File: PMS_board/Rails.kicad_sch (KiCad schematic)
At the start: 33 parts, among them J1 D1, J10 CORE, J11 DRIVE, J12 JET1, J13 AUX1, J14 AUX2, J15 JET2, J2 D2, J3 D3, J4 D4, J5 T1, J6 T2, J7 T3, J8 T4, J9 NET

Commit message: Add Footprints & such
whoops forgot to push yesterday teehee
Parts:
- added TP2: TestPoint, Relay_THT:Relay_DPDT_Schrack-RT2-FormC_RM5mm, symbol Connector:TestPoint
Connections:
- net AUX+: now also TP2.1
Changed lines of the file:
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@@
+	)
+	(junction
+		(at 137.16 120.65)
+		(diameter 0)
+		(color 0 0 0 0)
 	)
 	(junction
@@
 					(unit 1)
 				)
+			)
+		)
+	)
+	(symbol
+		(lib_id "Connector:TestPoint")
+		(at 137.16 120.65 0)
+		(unit 1)
+		(body_style 1)
+		(exclude_from_sim no)
+		(in_bom yes)
+		(on_board yes)
+		(in_pos_files yes)
+		(dnp no)
+		(fields_autoplaced yes)
+		(property "Reference" "TP2"
+			(at 139.7 116.0779 0)
+			(show_name no)
+			(do_not_autoplace no)
+			(effects
+				(font
+					(size 1.27 1.27)
+				)
+				(justify left)
+			)
+		)
+		(property "Value" "TestPoint"
+			(at 139.7 118.6179 0)
+			(show_name no)
+			(do_not_autoplace no)
+			(effects
+				(font
+					(size 1.27 1.27)
+				)
+				(justify left)
+			)
+		)
+		(property "Footprint" "Relay_THT:Relay_DPDT_Schrack-RT2-FormC_RM5mm"
+			(at 142.24 120.65 0)
+			(hide yes)
+			(show_name no)
+			(do_not_autoplace no)
+			(effects
+				(font
+					(size 1.27 1.27)
+				)
+			)
+		)
+		(property "Datasheet" ""
+			(at 142.24 120.65 0)
+			(hide yes)
+			(show_name no)
+			(do_not_autoplace no)
+			(effects
+				(font
+					(size 1.27 1.27)
+				)
+			)
+		)
+		(property "Description" "test point"
+			(at 137.16 120.65 0)
+			(hide yes)
+			(show_name no)
+			(do_not_autoplace no)
+			(effects
+				(font
+					(size 1.27 1.27)
+				)
+			)
+		)
+		(pin "1"
+		)
+		(instances
+			(project "PMS_board"
+				(path "/282246b0-e0d8-4997-b3ee-58bf10355d52/266cb597-81f7-4ea7-87c1-e1b826fc674e/1ce466be-8c1f-42c9-b575-af9917f46ea9"
+					(reference "TP2")
+					(unit 1)
+				)

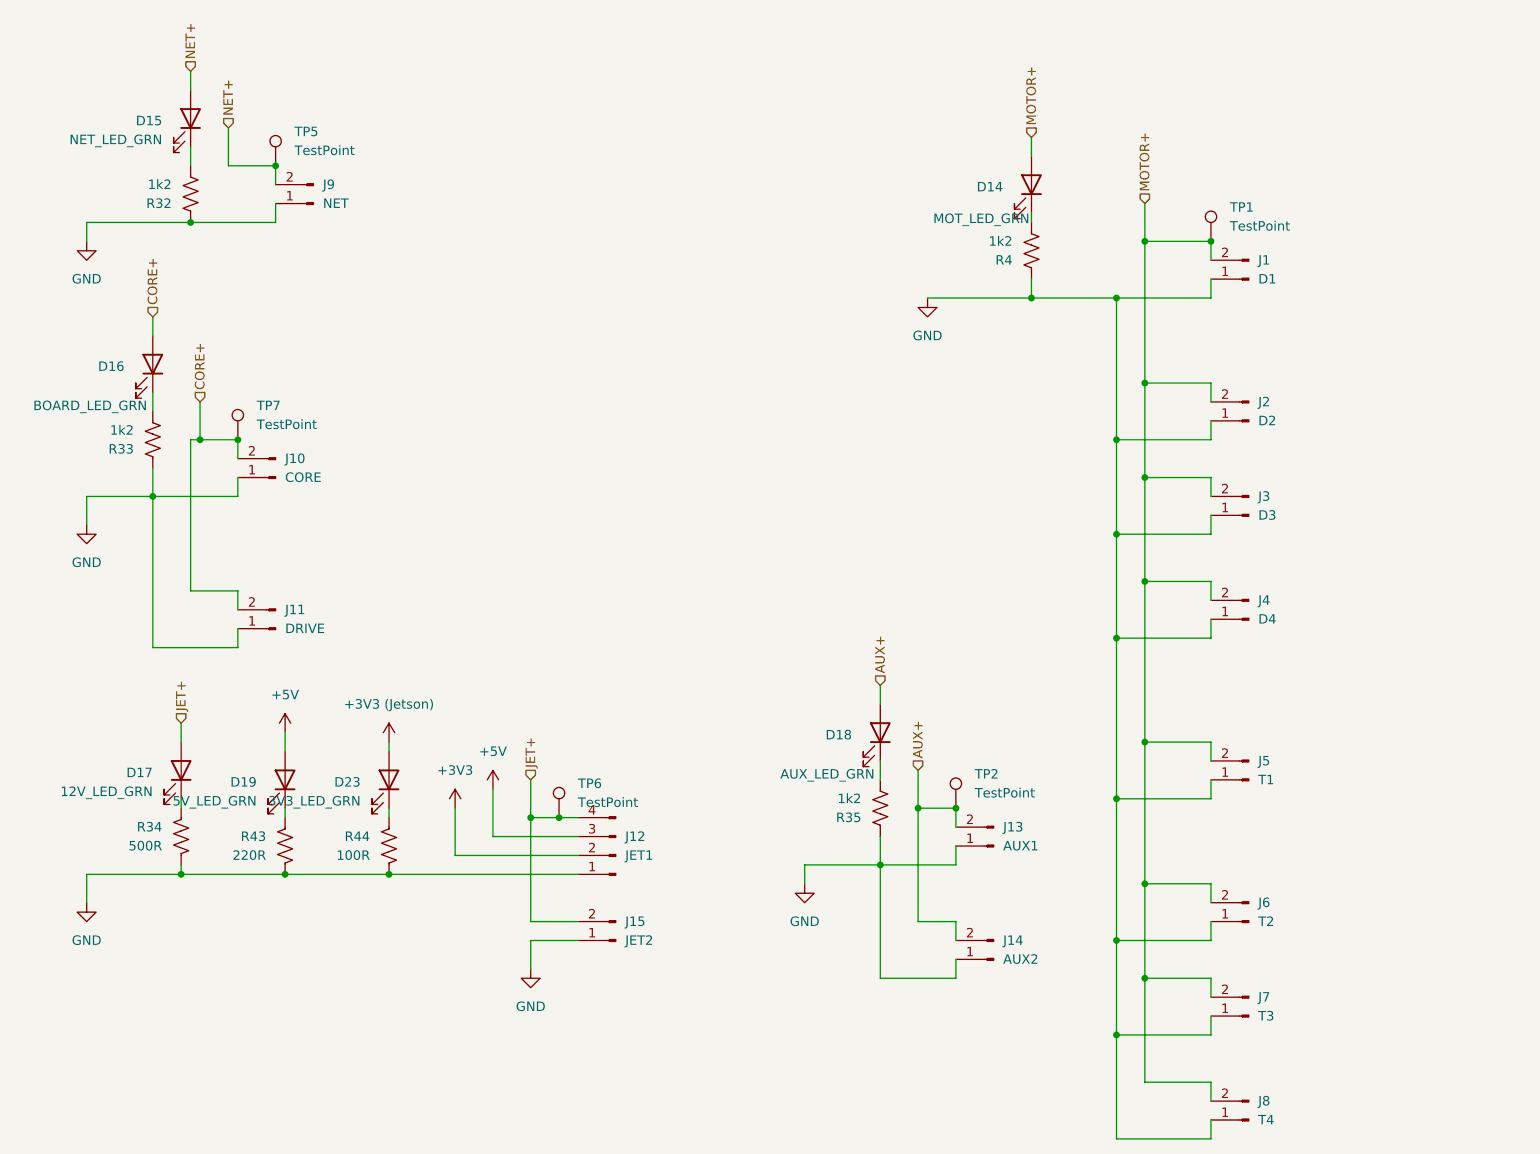
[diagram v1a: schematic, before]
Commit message: Minor component tweaks and added a seperate LED sheet
Changed component values
Added labels
Moved LEDs to it's own sheet
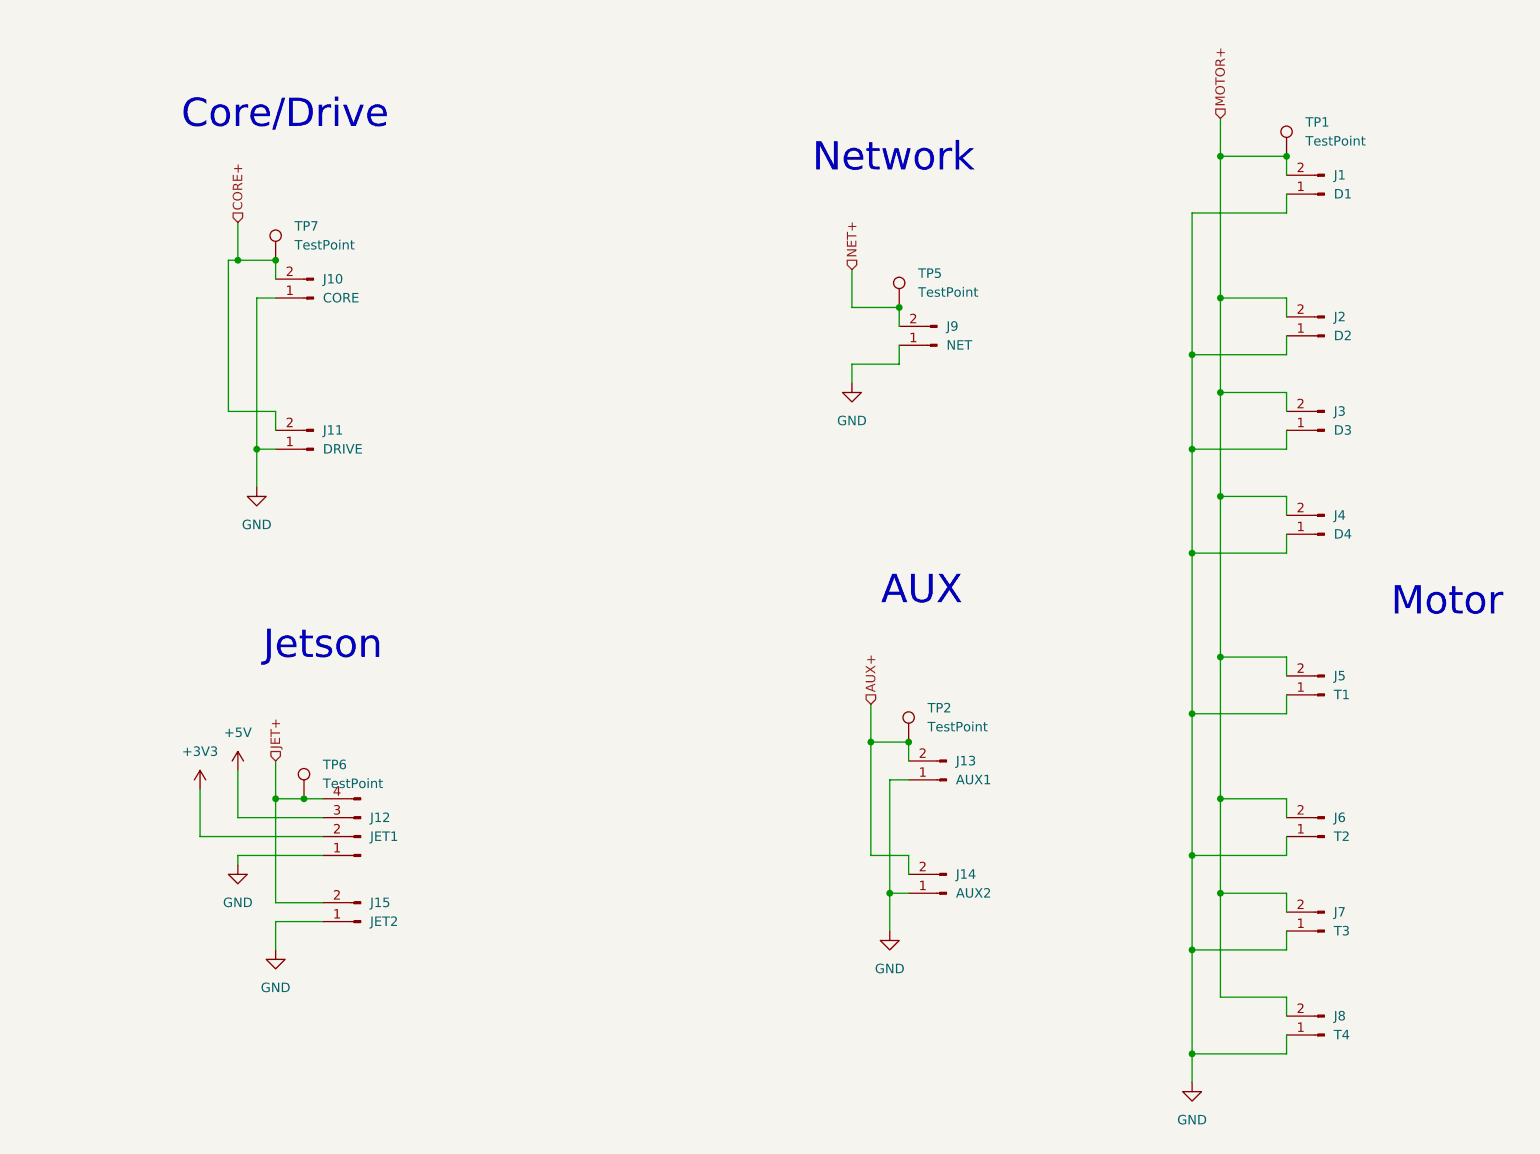
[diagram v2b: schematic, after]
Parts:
- removed D14: MOT_LED_GRN, LED_SMD:LED_Cree-XHP50_3V_HighDensity, symbol Device:LED
- removed D15: NET_LED_GRN, symbol Device:LED
- removed D16: BOARD_LED_GRN, symbol Device:LED
- removed D17: 12V_LED_GRN, symbol Device:LED
- removed D18: AUX_LED_GRN, symbol Device:LED
- removed D19: 5V_LED_GRN, symbol Device:LED
- removed D23: 3V3_LED_GRN, symbol Device:LED
- removed R32, R33, R35, R4: 1k2, symbol Device:R_US
- removed R34: 500R, symbol Device:R_US
- removed R43: 220R, symbol Device:R_US
- removed R44: 100R, symbol Device:R_US
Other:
- note added: "AUX"
- note added: "Core/Drive"
- note added: "Jetson"
- note added: "Motor"
- note added: "Network"
- moved on the sheet: J1, J10, J11, J12, J13, J14, J15, J2, J3, J4, J5, J6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

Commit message: How did our footprints get this geeked???
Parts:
- J1, J10, J11, J13, J14, J2, J3, J4, J5, J6, J7, J8, J9: footprint Connector:Tag-Connect_TC2030-IDC-FP_2x03_P1.27mm_Vertical -> (none)
- TP1, TP2, TP5, TP6, TP7: footprint Relay_THT:Relay_DPDT_Schrack-RT2-FormC_RM5mm -> (none)
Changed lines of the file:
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@@
 			)
 		)
-		(property "Footprint" "Connector:Tag-Connect_TC2030-IDC-FP_2x03_P1.27mm_Vertical"
+		(property "Footprint" ""
 			(at 50.8 52.07 0)
 			(hide yes)
@@
 			)
 		)
-		(property "Footprint" "Connector:Tag-Connect_TC2030-IDC-FP_2x03_P1.27mm_Vertical"
+		(property "Footprint" ""
 			(at 186.69 151.13 0)
 			(hide yes)
@@
 			)
 		)
-		(property "Footprint" "Relay_THT:Relay_DPDT_Schrack-RT2-FormC_RM5mm"
+		(property "Footprint" ""
 			(at 135.89 111.76 0)
 			(hide yes)
@@
 			)
 		)
-		(property "Footprint" "Connector:Tag-Connect_TC2030-IDC-FP_2x03_P1.27mm_Vertical"
+		(property "Footprint" ""
 			(at 186.69 124.46 0)
 			(hide yes)
@@
 			)
 		)
-		(property "Footprint" "Connector:Tag-Connect_TC2030-IDC-FP_2x03_P1.27mm_Vertical"
+		(property "Footprint" ""
 			(at 186.69 105.41 0)
 			(hide yes)
@@
 			)
 		)
-		(property "Footprint" "Connector:Tag-Connect_TC2030-IDC-FP_2x03_P1.27mm_Vertical"
+		(property "Footprint" ""
 			(at 134.62 58.42 0)
 			(hide yes)
@@
 			)
 		)
-		(property "Footprint" "Relay_THT:Relay_DPDT_Schrack-RT2-FormC_RM5mm"
+		(property "Footprint" ""
 			(at 186.69 33.02 0)
 			(hide yes)
@@
 			)
 		)
-		(property "Footprint" "Connector:Tag-Connect_TC2030-IDC-FP_2x03_P1.27mm_Vertical"
+		(property "Footprint" ""
 			(at 186.69 83.82 0)
 			(hide yes)
@@
 			)
 		)
-		(property "Footprint" "Connector:Tag-Connect_TC2030-IDC-FP_2x03_P1.27mm_Vertical"
+		(property "Footprint" ""
 			(at 186.69 38.1 0)
 			(hide yes)
@@
 			)
 		)
-		(property "Footprint" "Connector:Tag-Connect_TC2030-IDC-FP_2x03_P1.27mm_Vertical"
+		(property "Footprint" ""
 			(at 135.89 132.08 0)
 			(hide yes)
@@
 			)
 		)
-		(property "Footprint" "Relay_THT:Relay_DPDT_Schrack-RT2-FormC_RM5mm"
+		(property "Footprint" ""
 			(at 50.8 46.99 0)
 			(hide yes)
@@
 			)
 		)
-		(property "Footprint" "Connector:Tag-Connect_TC2030-IDC-FP_2x03_P1.27mm_Vertical"
+		(property "Footprint" ""
 			(at 186.69 69.85 0)
 			(hide yes)
@@
 			)
 		)
-		(property "Footprint" "Relay_THT:Relay_DPDT_Schrack-RT2-FormC_RM5mm"
+		(property "Footprint" ""
 			(at 134.62 53.34 0)
 			(hide yes)
@@
 			)
 		)
-		(property "Footprint" "Connector:Tag-Connect_TC2030-IDC-FP_2x03_P1.27mm_Vertical"
+		(property "Footprint" ""
 			(at 186.69 57.15 0)
 			(hide yes)
@@
 			)
 		)
-		(property "Footprint" "Connector:Tag-Connect_TC2030-IDC-FP_2x03_P1.27mm_Vertical"
+		(property "Footprint" ""
 			(at 186.69 137.16 0)
 			(hide yes)
@@
 			)
 		)
-		(property "Footprint" "Relay_THT:Relay_DPDT_Schrack-RT2-FormC_RM5mm"
+		(property "Footprint" ""
 			(at 54.61 119.38 0)
 			(hide yes)
@@
 			)
 		)
-		(property "Footprint" "Connector:Tag-Connect_TC2030-IDC-FP_2x03_P1.27mm_Vertical"
+		(property "Footprint" ""
 			(at 135.89 116.84 0)
 			(hide yes)
@@
 			)
 		)
-		(property "Footprint" "Connector:Tag-Connect_TC2030-IDC-FP_2x03_P1.27mm_Vertical"
+		(property "Footprint" ""
 			(at 50.8 72.39 0)
 			(hide yes)
